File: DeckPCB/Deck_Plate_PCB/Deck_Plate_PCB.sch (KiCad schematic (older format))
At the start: 52 parts, among them J1 Raspberry_Pi_2_3, J2 NASA_Telemetry_Interface, J3 NASA PWR_Interface, J8 Board_to_Board, J9 Power, P1 Digital, P10 CONN_01X01, P11 CONN_01X01, P12 CONN_01X01, P13 CONN_01X01, P2 Power, P3 Analog, P4 Analog, P5 PWM, P6 PWM, P7 Communication, P8 CONN_01X01, P9 CONN_01X01, Q2 2N7000, Q3 2N7000, U2 LM2576T-5, U3 D24V25F9, U5 LM2576T-5, U6 SF_Logic_Level_Conv, U7 Lidar_RangeFinder, U8 ADXL377, U9 TTL_Camera

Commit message: Finised routing fro Main_Board, Daughter_Board, and BurnWire circuits. Creating SensorEndPanel board next.
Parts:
- J9: footprint Connector_PinHeader_2.54mm:PinHeader_1x03_P2.54mm_Vertical -> Connector_PinHeader_2.54mm:PinHeader_1x04_P2.54mm_Vertical; symbol Connector:Conn_01x03_Male -> Connector:Conn_01x04_Male
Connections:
- net labels removed: +5V
- no-connect marks 111 -> 113
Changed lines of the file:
@@
 Reset
-$Comp
-L power:+5V #PWR02
-U 1 1 56D71D10
-P 9000 1050
-F 0 "#PWR02" H 9000 900 50  0001 C CNN
-F 1 "+5V" V 9000 1250 50  0000 C CNN
-F 2 "" H 9000 1050 50  0000 C CNN
-F 3 "" H 9000 1050 50  0000 C CNN
-	1    9000 1050
-	1    0    0    -1
-$EndComp
 $Comp
 L power:GND #PWR03
@@
 Wire Wire Line
 	10750 4850 10600 4850
-$Comp
-L power:+5V #PWR06
-U 1 1 56D75AB8
-P 10750 4550
-F 0 "#PWR06" H 10750 4400 50  0001 C CNN
-F 1 "+5V" H 10750 4690 50  0000 C CNN
-F 2 "" H 10750 4550 50  0000 C CNN
-F 3 "" H 10750 4550 50  0000 C CNN
-	1    10750 4550
-	1    0    0    -1
-$EndComp
 Connection ~ 10750 4850
 Wire Wire Line
@@
 SDA
 $Comp
-L Connector:Conn_01x03_Male J9
+L Connector:Conn_01x04_Male J9
 U 1 1 5E677FD9
 P 3650 1750
 F 0 "J9" V 3900 1900 50  0000 L CNN
 F 1 "Power" V 3600 1600 50  0000 L CNN
-F 2 "Connector_PinHeader_2.54mm:PinHeader_1x03_P2.54mm_Vertical" H 3650 1750 50  0001 C CNN
+F 2 "Connector_PinHeader_2.54mm:PinHeader_1x04_P2.54mm_Vertical" H 3650 1750 50  0001 C CNN
 F 3 "~" H 3650 1750 50  0001 C CNN
 	1    3650 1750
@@
 NoConn ~ 6300 1150
 NoConn ~ 6300 1250
+NoConn ~ 9000 1050
+NoConn ~ 10750 4550
+$Comp
+L power:GND #PWR?
+U 1 1 5E6AE9BE
+P 3450 1950
+F 0 "#PWR?" H 3450 1700 50  0001 C CNN
+F 1 "GND" H 3455 1777 50  0000 C CNN
+F 2 "" H 3450 1950 50  0001 C CNN
+F 3 "" H 3450 1950 50  0001 C CNN
+	1    3450 1950
+	1    0    0    -1
+$EndComp
 $EndSCHEMATC

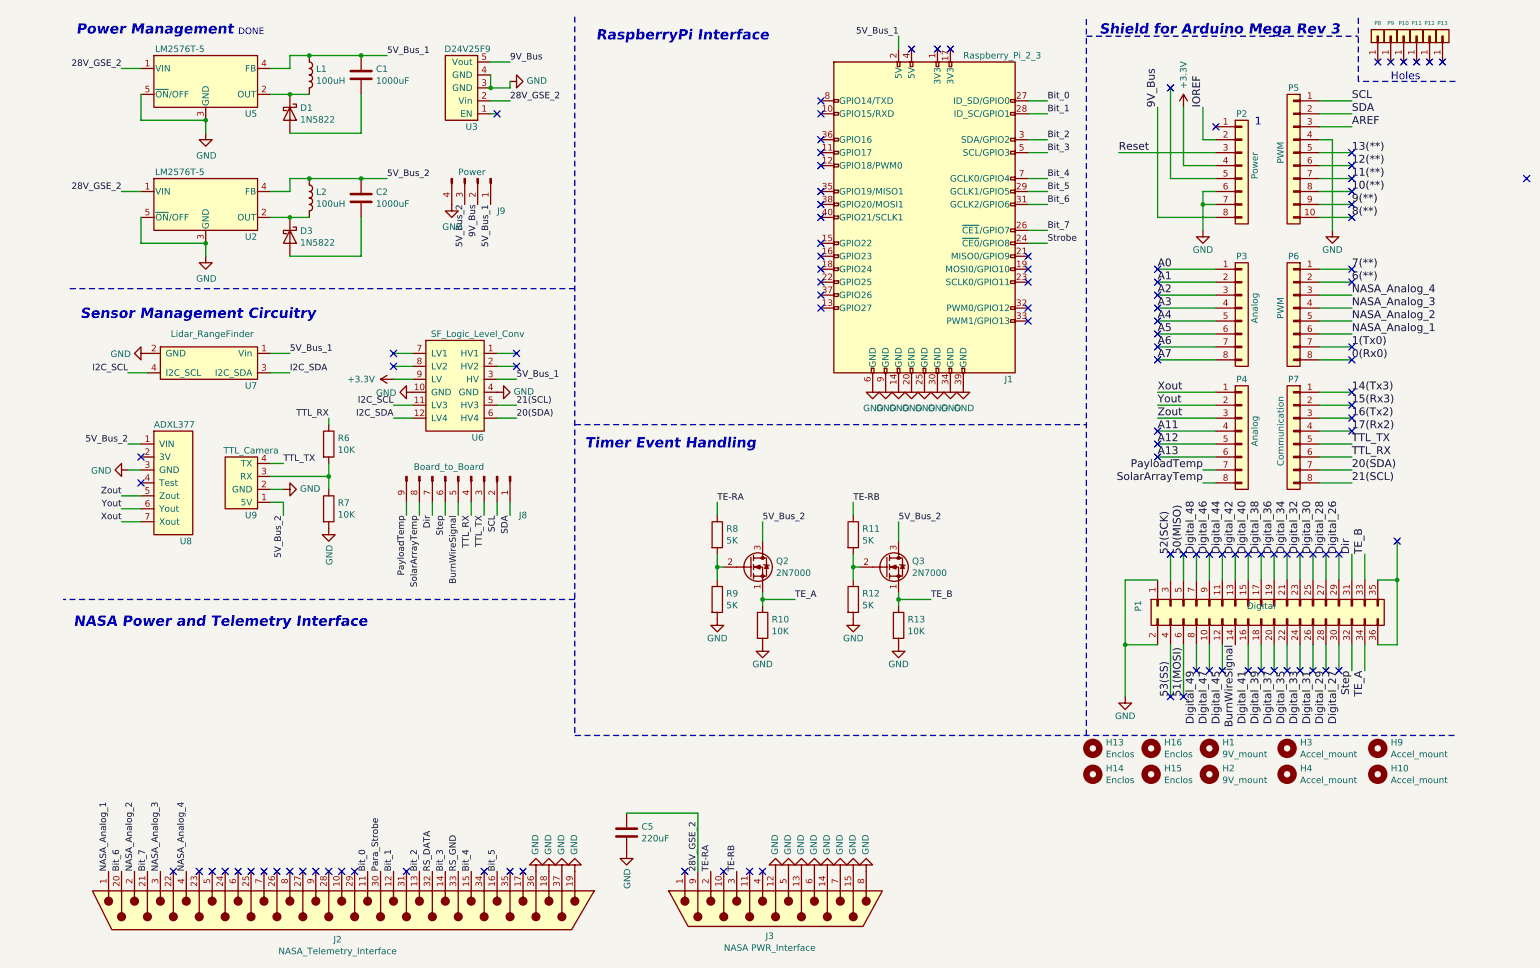
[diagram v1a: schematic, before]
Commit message: Added signal conditioning circuitry
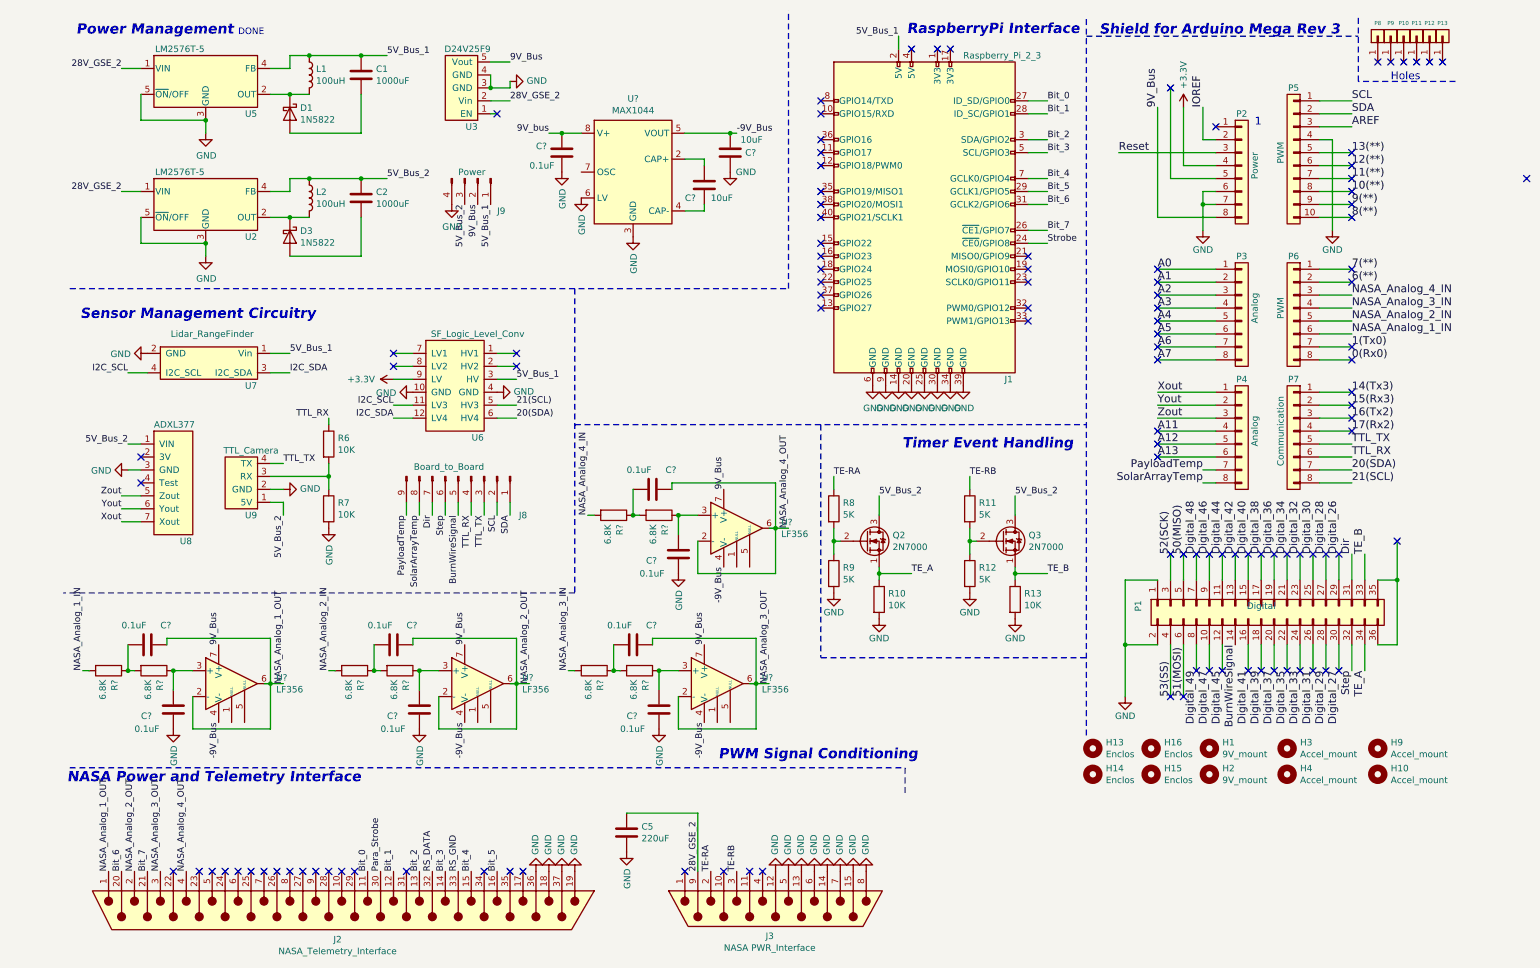
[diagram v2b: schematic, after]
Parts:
- added C? (x9): 0.1uF, Capacitor_THT:C_Axial_L3.8mm_D2.6mm_P7.50mm_Horizontal, symbol Device:C
- added C? (x2): 10uF, Capacitor_THT:C_Axial_L3.8mm_D2.6mm_P7.50mm_Horizontal, symbol Device:C
- added R? (x8): 6.8K, Resistor_THT:R_Axial_DIN0207_L6.3mm_D2.5mm_P10.16mm_Horizontal, symbol Device:R
- added U? (x4): LF356, symbol Amplifier_Operational:LF356
- added U?: MAX1044, Package_DIP:DIP-8_W7.62mm, symbol Regulator_SwitchedCapacitor:MAX1044
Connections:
- net 9V_Bus: now also U?.7 (V+), U?.7 (V+), U?.7 (V+), U?.7 (V+)
- net GND: now also C?.1, C?.2, C?.2, C?.2, C?.2, C?.2, U?.3 (GND), U?.6 (LV)
- net NASA_Analog_1 renamed NASA_Analog_1_IN
- net NASA_Analog_1_IN: now also R?.2; no longer J2.1
- net NASA_Analog_2 renamed NASA_Analog_2_IN
- net NASA_Analog_2_IN: now also R?.2; no longer J2.2
- net NASA_Analog_3 renamed NASA_Analog_3_IN
- net NASA_Analog_3_IN: now also R?.2; no longer J2.3
- net NASA_Analog_4 renamed NASA_Analog_4_IN
- net NASA_Analog_4_IN: now also R?.2; no longer J2.4
- new net: C?.1, R?.1, U?.3 (+) (x4)
- new net: C?.2, R?.1, R?.2 (x4)
- new net: C?.1, U?.2 (CAP+)
- new net: C?.2, U?.4 (CAP-)
- new net -9V_Bus: C?.2, U?.4 (V-), U?.4 (V-), U?.4 (V-), U?.4 (V-), U?.5 (VOUT)
- new net 9V_bus: C?.1, U?.8 (V+)
- new net NASA_Analog_1_OUT: C?.1, J2.1, U?.2 (-), U?.6
- new net NASA_Analog_2_OUT: C?.1, J2.2, U?.2 (-), U?.6
- new net NASA_Analog_3_OUT: C?.1, J2.3, U?.2 (-), U?.6
- new net NASA_Analog_4_OUT: C?.1, J2.4, U?.2 (-), U?.6
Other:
- note added: "PWM Signal Conditioning\n\n\n"
- moved on the sheet: Q2, Q3, R10, R11, R12, R13, R8, R9

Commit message: Added signal conditioning circuitry and finalized main deck PCB component placement and signal tracing
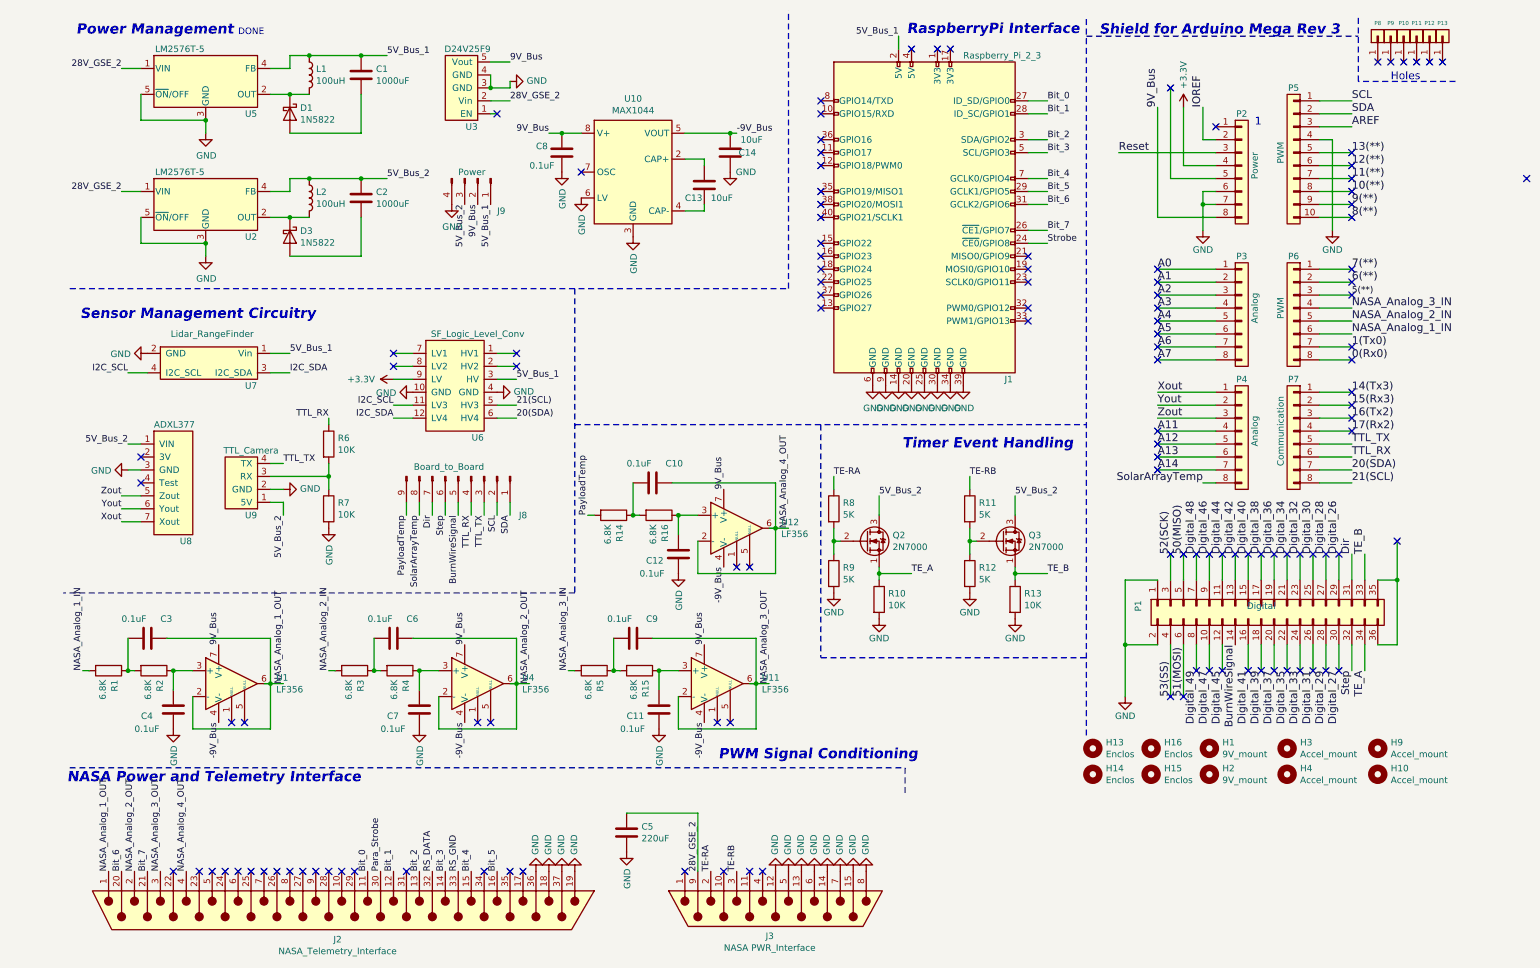
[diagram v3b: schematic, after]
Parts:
- U1, U11, U12, U4: renamed from U?; footprint (none) -> Package_DIP:DIP-8_W7.62mm
- gave numbers to parts that had none: 20
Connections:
- net 9V_bus is gone; now on net 9V_Bus: C8.1, U10.8 (V+)
- net PayloadTemp: now also R14.2; no longer P4.7 (Pin_7)
- net NASA_Analog_4_IN renamed 5(**)
- net 5(**): no longer R14.2
- new net A14: P4.7 (Pin_7)
- no-connect marks 113 -> 124
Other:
- moved on the sheet: C10, C3, C6, C9

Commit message: Updated main board to incorporate all 16-bits of telemetry lines
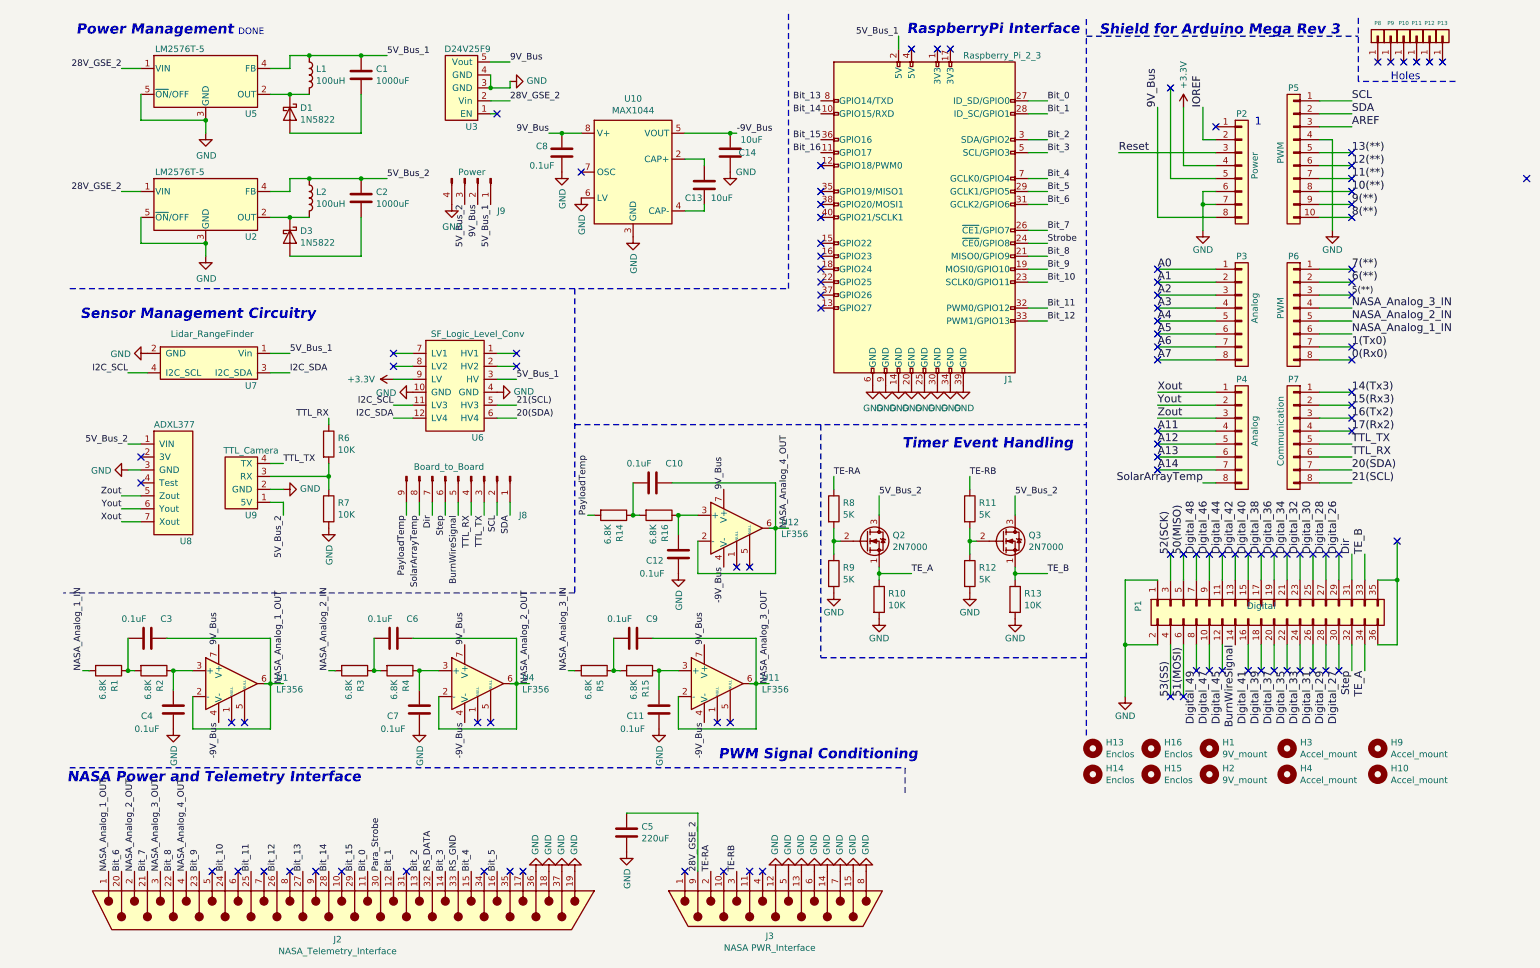
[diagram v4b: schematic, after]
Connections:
- net Bit_14: now reaches J1.10 (GPIO15/RXD)
- net Bit_14: now also J2.28
- net Bit_16: now reaches J1.11 (GPIO17)
- net Bit_9: now reaches J1.19 (MOSI0/GPIO10)
- net Bit_9: now also J2.23
- net Bit_8: now reaches J1.21 (MISO0/GPIO9)
- net Bit_8: now also J2.22
- net Bit_10: now reaches J1.23 (SCLK0/GPIO11)
- net Bit_10: now also J2.24
- net Bit_11: now reaches J1.32 (PWM0/GPIO12)
- net Bit_11: now also J2.25
- net Bit_12: now reaches J1.33 (PWM1/GPIO13)
- net Bit_12: now also J2.26
- net Bit_15: now reaches J1.36 (GPIO16)
- net Bit_15: now also J2.29
- net Bit_13: now reaches J1.8 (GPIO14/TXD)
- net Bit_13: now also J2.27
- no-connect marks 124 -> 107
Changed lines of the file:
@@
-$EndComp
-$Comp
-L Connector:DB37_Male J2
-U 1 1 5E4749AA
-P 2600 7400
-F 0 "J2" V 2825 7368 50  0000 C CNN
-F 1 "NASA_Telemetry_Interface" V 2916 7368 50  0000 C CNN
-F 2 "Deck_Plate_PCB:NASA_Telem_37-pin_DSub" H 2600 7400 50  0001 C CNN
-F 3 " ~" H 2600 7400 50  0001 C CNN
-	1    2600 7400
-	0    1    1    0
 $EndComp
 $Comp
@@
 Wire Wire Line
 	7900 1450 8050 1450
-NoConn ~ 7900 2750
-NoConn ~ 6300 1450
-NoConn ~ 7900 2850
-NoConn ~ 7900 2550
-NoConn ~ 7900 2450
 NoConn ~ 7000 750
 NoConn ~ 6300 1650
-NoConn ~ 6300 1550
 NoConn ~ 6300 2750
 NoConn ~ 7300 750
@@
 NoConn ~ 6300 2550
 NoConn ~ 6300 2650
-NoConn ~ 7900 2350
 NoConn ~ 11750 1750
 Text Label 9600 5550 3    60   ~ 0
@@
 Text Label 2200 3100 0    50   ~ 0
 5V_Bus_1
-NoConn ~ 1300 7100
-NoConn ~ 1500 7100
-NoConn ~ 1600 7100
-NoConn ~ 1700 7100
-NoConn ~ 1800 7100
-NoConn ~ 1900 7100
-NoConn ~ 2000 7100
-NoConn ~ 2100 7100
 NoConn ~ 2200 7100
-NoConn ~ 2300 7100
 NoConn ~ 2400 7100
-NoConn ~ 2500 7100
-NoConn ~ 2600 7100
-NoConn ~ 2700 7100
 NoConn ~ 5250 7100
 NoConn ~ 5850 7100
@@
 Text Label 1100 7100 1    50   ~ 0
 Bit_7
-NoConn ~ 6300 1150
-NoConn ~ 6300 1250
 NoConn ~ 9000 1050
 NoConn ~ 10750 4550
@@
 	8900 4000 9350 4000
 NoConn ~ 8900 4000
+$Comp
+L Connector:DB37_Male J2
+U 1 1 5E4749AA
+P 2600 7400
+F 0 "J2" V 2825 7368 50  0000 C CNN
+F 1 "NASA_Telemetry_Interface" V 2916 7368 50  0000 C CNN
+F 2 "Deck_Plate_PCB:NASA_Telem_37-pin_DSub" H 2600 7400 50  0001 C CNN
+F 3 " ~" H 2600 7400 50  0001 C CNN
+	1    2600 7400
+	0    1    1    0
+$EndComp
+Text Label 1300 7100 1    50   ~ 0
+Bit_8
+Text Label 1500 7100 1    50   ~ 0
+Bit_9
+NoConn ~ 2000 7100
+NoConn ~ 1800 7100
+NoConn ~ 1600 7100
+Text Label 1700 7100 1    50   ~ 0
+Bit_10
+Text Label 1900 7100 1    50   ~ 0
+Bit_11
+Text Label 2100 7100 1    50   ~ 0
+Bit_12
+Text Label 2300 7100 1    50   ~ 0
+Bit_13
+Text Label 2500 7100 1    50   ~ 0
+Bit_14
+Text Label 2700 7100 1    50   ~ 0
+Bit_15
+NoConn ~ 2600 7100
+Text Label 8050 2350 0    50   ~ 0
+Bit_8
+Text Label 8050 2450 0    50   ~ 0
+Bit_9
+Text Label 8050 2550 0    50   ~ 0
+Bit_10
+Text Label 8050 2750 0    50   ~ 0
+Bit_11
+Text Label 8050 2850 0    50   ~ 0
+Bit_12
+Text Label 6300 1150 2    50   ~ 0
+Bit_13
+Text Label 6300 1250 2    50   ~ 0
+Bit_14
+Text Label 6300 1450 2    50   ~ 0
+Bit_15
+Text Label 6300 1550 2    50   ~ 0
+Bit_16
+Wire Wire Line
+	7900 2350 8050 2350
+Wire Wire Line
+	7900 2450 8050 2450
+Wire Wire Line
+	7900 2550 8050 2550
+Wire Wire Line
+	7900 2750 8050 2750
+Wire Wire Line
+	7900 2850 8050 2850
 $EndSCHEMATC
